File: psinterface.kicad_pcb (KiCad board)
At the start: 2 copper layers, 74.8 x 45 mm, 7 parts, among them J1 Conn_02x04_Top_Bottom, J2 Conn_01x10, J3 Conn_02x06_Top_Bottom, J4 Conn_01x05, J5 Conn_01x01, J6 Conn_01x03, SW1 SW_SPDT

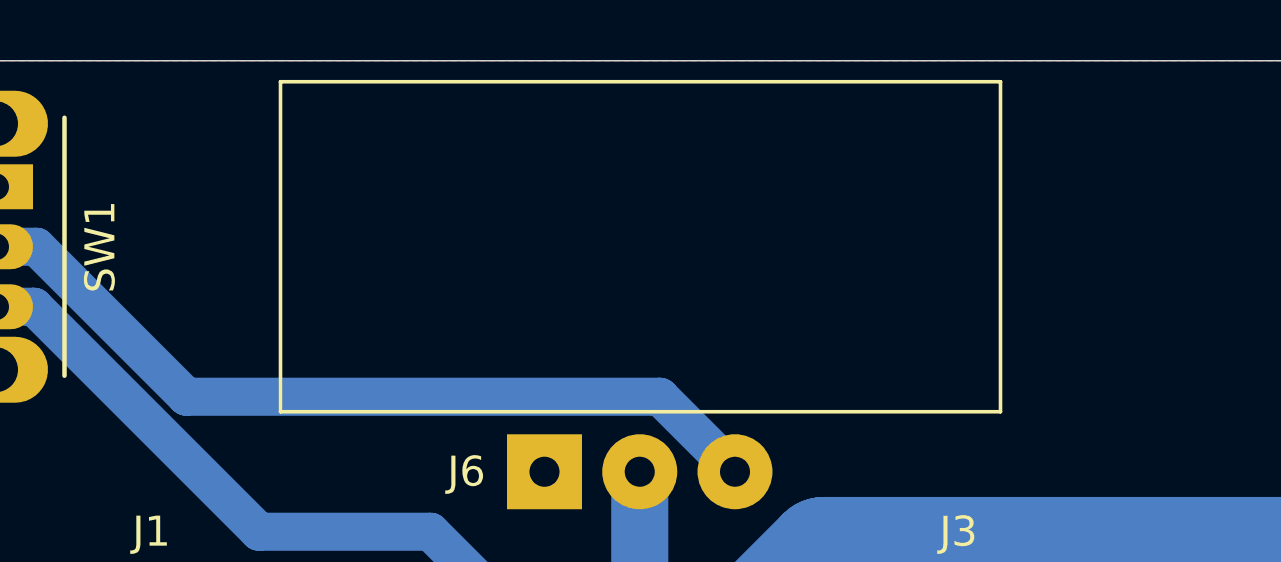
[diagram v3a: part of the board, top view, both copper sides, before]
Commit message: Mounting holes for LCD fixed
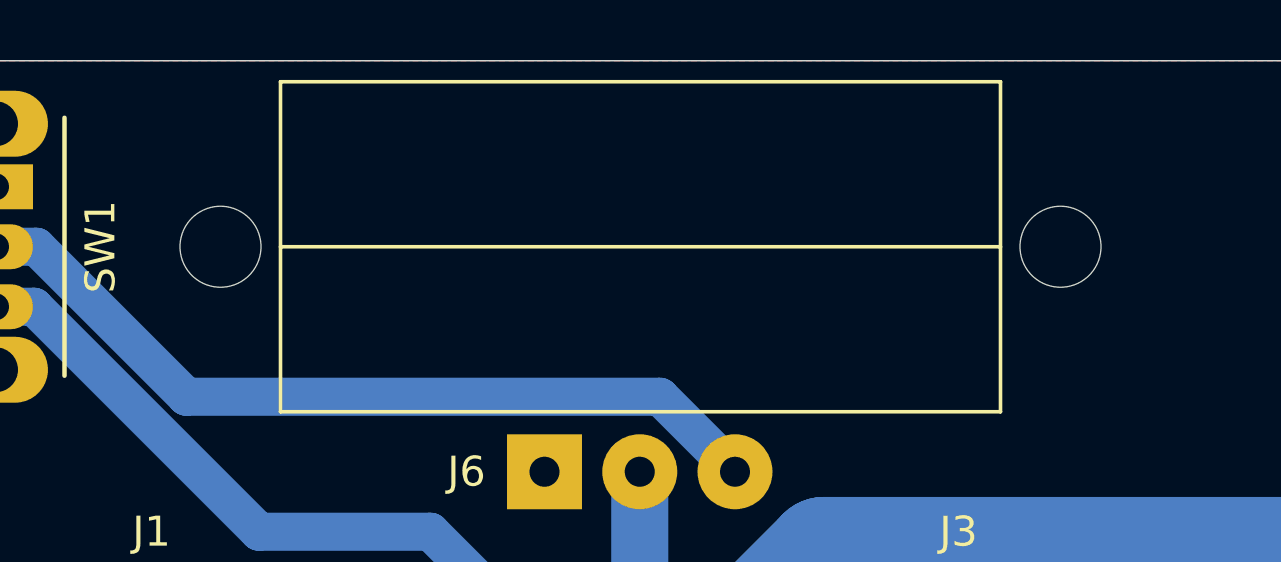
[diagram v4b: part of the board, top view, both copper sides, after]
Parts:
- added H1: MountingHole, MountingHole:MountingHole_2.7mm_M2.5, F.Cu at (115.0, 100.5)
- added H2: MountingHole, MountingHole:MountingHole_2.7mm_M2.5, F.Cu at (143.0, 100.5)
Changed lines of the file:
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@@
   (general
     (thickness 1.6)
-    (drawings 57)
+    (drawings 58)
     (tracks 74)
     (zones 0)
-    (modules 7)
+    (modules 9)
     (nets 10)
   )
@@
       (net 9 "Net-(J6-Pad3)"))
   )
+  (module MountingHole:MountingHole_2.7mm_M2.5 (layer F.Cu)
+    (at 115 100.5)
+    (descr "Mounting Hole 2.7mm, no annular, M2.5")
+    (tags "mounting hole 2.7mm no annular m2.5")
+    (attr virtual)
+    (fp_text reference H1 (at 0 -3.7) (layer F.SilkS) hide
+      (effects (font (size 1 1) (thickness 0.15)))
+    )
+    (fp_text value MountingHole (at 0 3.7) (layer F.Fab)
+      (effects (font (size 1 1) (thickness 0.15)))
+    )
+    (fp_text user %R (at 0.3 0) (layer F.Fab)
+      (effects (font (size 1 1) (thickness 0.15)))
+    )
+    (fp_circle (center 0 0) (end 2.7 0) (layer Cmts.User) (width 0.15))
+    (fp_circle (center 0 0) (end 2.95 0) (layer F.CrtYd) (width 0.05))
+    (pad 1 np_thru_hole circle (at 0 0) (size 2.7 2.7) (drill 2.7) (layers *.Cu *.Mask))
+  )
+  (module MountingHole:MountingHole_2.7mm_M2.5 (layer F.Cu)
+    (at 143 100.5)
+    (descr "Mounting Hole 2.7mm, no annular, M2.5")
+    (tags "mounting hole 2.7mm no annular m2.5")
+    (attr virtual)
+    (fp_text reference H2 (at 0 -3.7) (layer F.SilkS) hide
+      (effects (font (size 1 1) (thickness 0.15)))
+    )
+    (fp_text value MountingHole (at 0 3.7) (layer F.Fab)
+      (effects (font (size 1 1) (thickness 0.15)))
+    )
+    (fp_circle (center 0 0) (end 2.95 0) (layer F.CrtYd) (width 0.05))
+    (fp_circle (center 0 0) (end 2.7 0) (layer Cmts.User) (width 0.15))
+    (fp_text user %R (at 0.3 0) (layer F.Fab)
+      (effects (font (size 1 1) (thickness 0.15)))
+    )
+    (pad 1 np_thru_hole circle (at 0 0) (size 2.7 2.7) (drill 2.7) (layers *.Cu *.Mask))
+  )
+  (gr_line (start 141 100.5) (end 117 100.5) (layer F.SilkS) (width 0.12))
   (gr_text "Meanwell\nQP-150-3A\nAWSD Interface" (at 168 97.5) (layer F.SilkS)
     (effects (font (size 1 1) (thickness 0.15)))

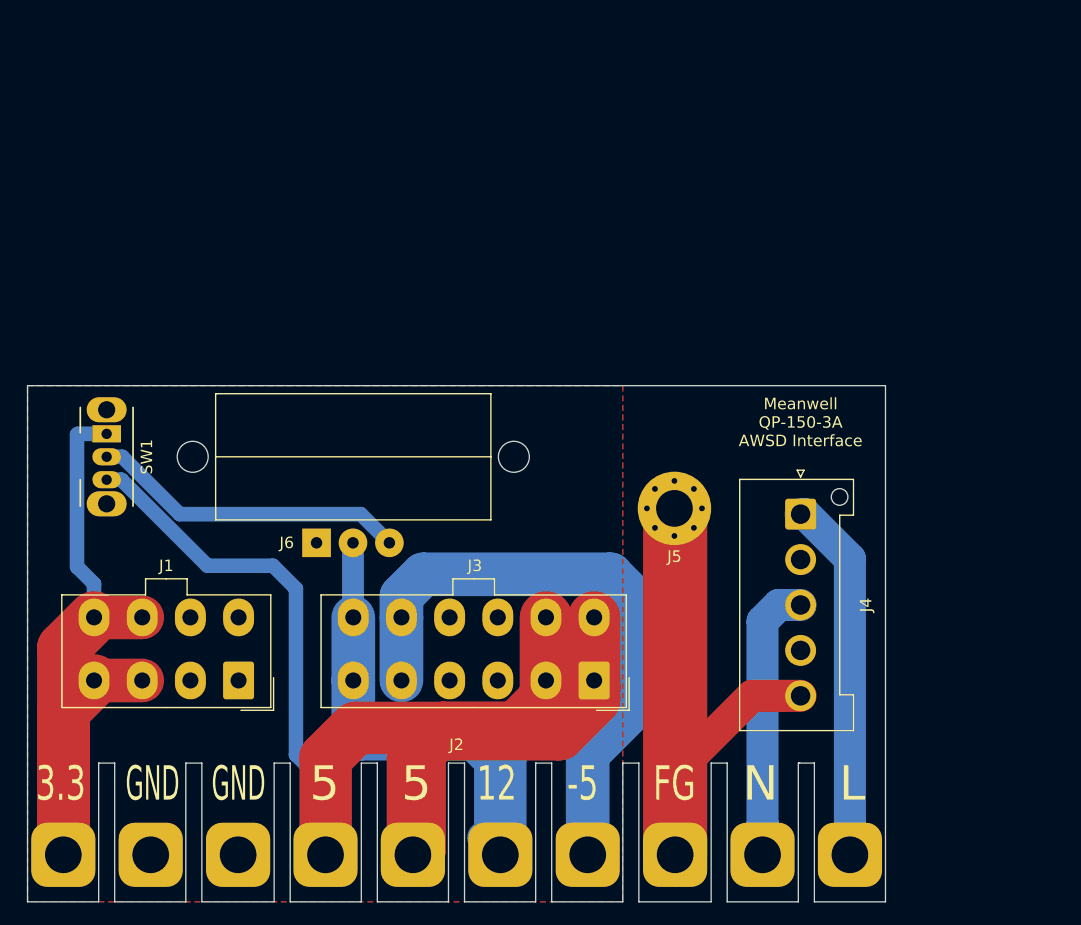
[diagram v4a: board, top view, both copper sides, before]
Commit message: Rounded flanges, fixed wiring
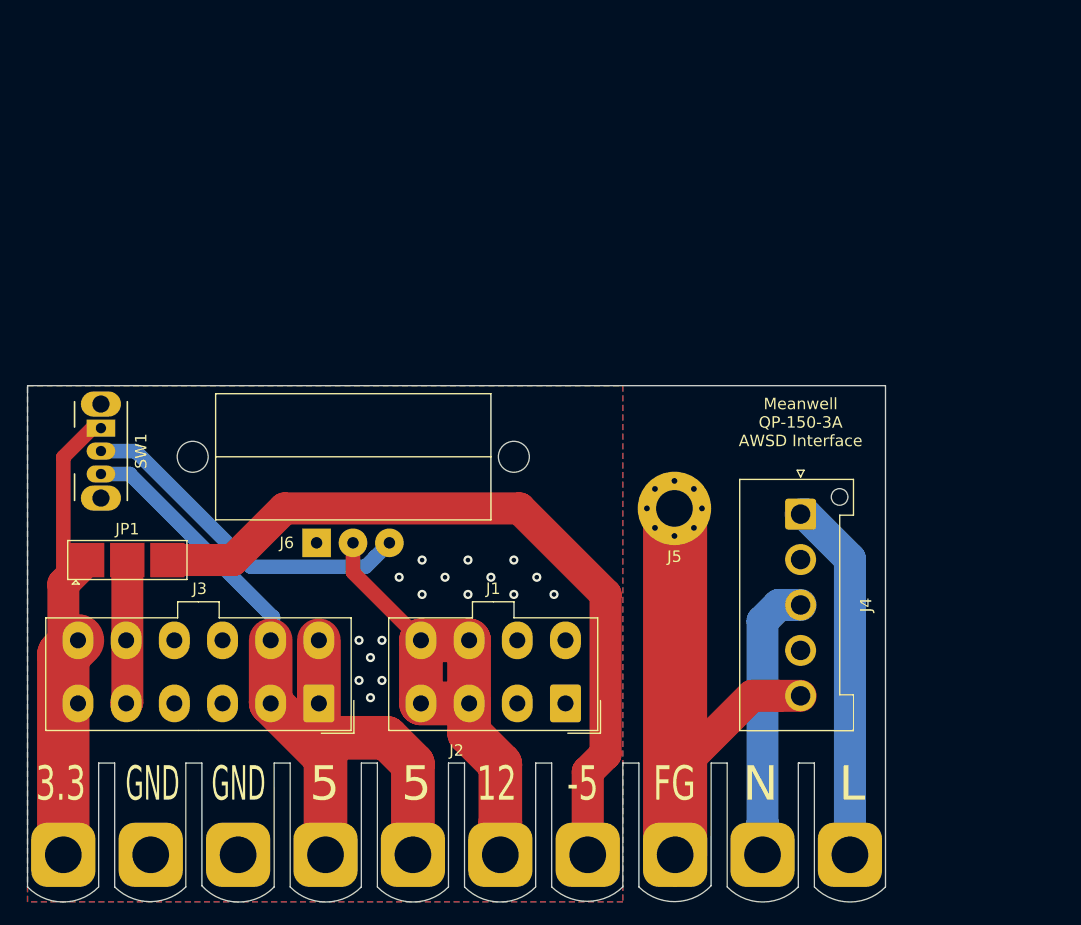
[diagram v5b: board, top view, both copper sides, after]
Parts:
- added JP1: SolderJumper_3_Open, Andrew-Custom:SolderJumper-3_P3.5mm_Open_Pad3.0x3.0mm, F.Cu at (109.3, 109.5)
- moved J1 28.6 mm to (147.5, 122.0)
- moved J3 24.1 mm to (126.0, 122.0)
- moved SW1 0.71 mm to (107.0, 98.0)
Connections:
- net Net-(J1-Pad1) renamed /GND
- net Net-(J2-Pad10) renamed /AC-L
- net Net-(J2-Pad4) renamed /5.25V
- net Net-(J2-Pad8) renamed /AC-FG
- net Net-(J2-Pad9) renamed /AC-N
- J1 pad 3: Net-(J1-Pad3) -> /12V
- J1 pad 4: Net-(J1-Pad3) -> /12V
- J1 pad 7: Net-(J1-Pad3) -> /12V
- J1 pad 8: Net-(J1-Pad3) -> /12V
- J2 pad 1: Net-(J1-Pad3) -> /3.3V
- J2 pad 6: Net-(J2-Pad6) -> /12V
- J2 pad 7: Net-(J2-Pad7) -> /-5V
- J3 pad 11: Net-(J2-Pad7) -> Net-(J3-Pad11)
- J3 pad 12: Net-(J2-Pad6) -> /3.3V
- J3 pad 5: Net-(J2-Pad7) -> Net-(J3-Pad11)
- J3 pad 6: Net-(J2-Pad6) -> /3.3V
- J6 pad 2: Net-(J2-Pad6) -> /12V
- SW1 pad 1: Net-(J1-Pad3) -> /3.3V
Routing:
- net /3.3V: track 0.00 -> 84.8 mm
- net /5.25V: track 142.6 -> 68.2 mm
- net /-5V: track 0.00 -> 66.5 mm
- net Net-(J1-Pad3): track 65.7 -> 0.00 mm
- net Net-(J2-Pad7): track 53.3 -> 0.00 mm
- net /12V: track 0.00 -> 44.7 mm
- net Net-(J2-Pad6): track 40.6 -> 0.00 mm
- net Net-(J3-Pad11): track 0.00 -> 12.5 mm
- net Net-(J6-Pad3): track 27.8 -> 30.2 mm
- net /GND: vias 0 -> 17
- added copper zone on B.Cu, net /GND
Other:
- outline, holes or cut-outs redrawn

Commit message: Better use of bottom copper
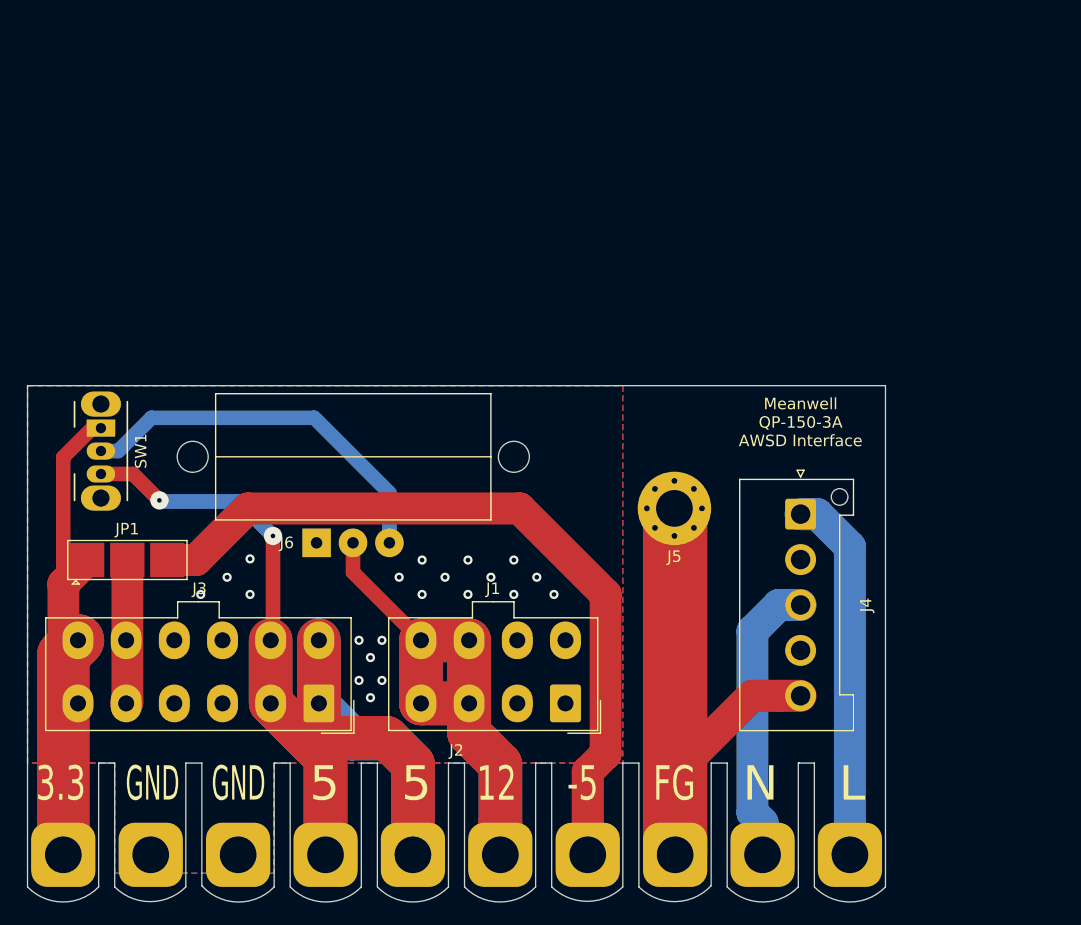
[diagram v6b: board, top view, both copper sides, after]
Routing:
- net /5.25V: track 68.2 -> 117.3 mm, vias 0 -> 2
- net /12V: track 44.7 -> 78.4 mm
- net /AC-FG: track 51.1 -> 81.3 mm
- net /3.3V: track 84.8 -> 104.0 mm
- net Net-(J6-Pad3): track 30.2 -> 33.4 mm
- net /AC-N: track 24.3 -> 25.0 mm
- net /AC-L: track 31.7 -> 32.3 mm
- net /GND: vias 17 -> 21

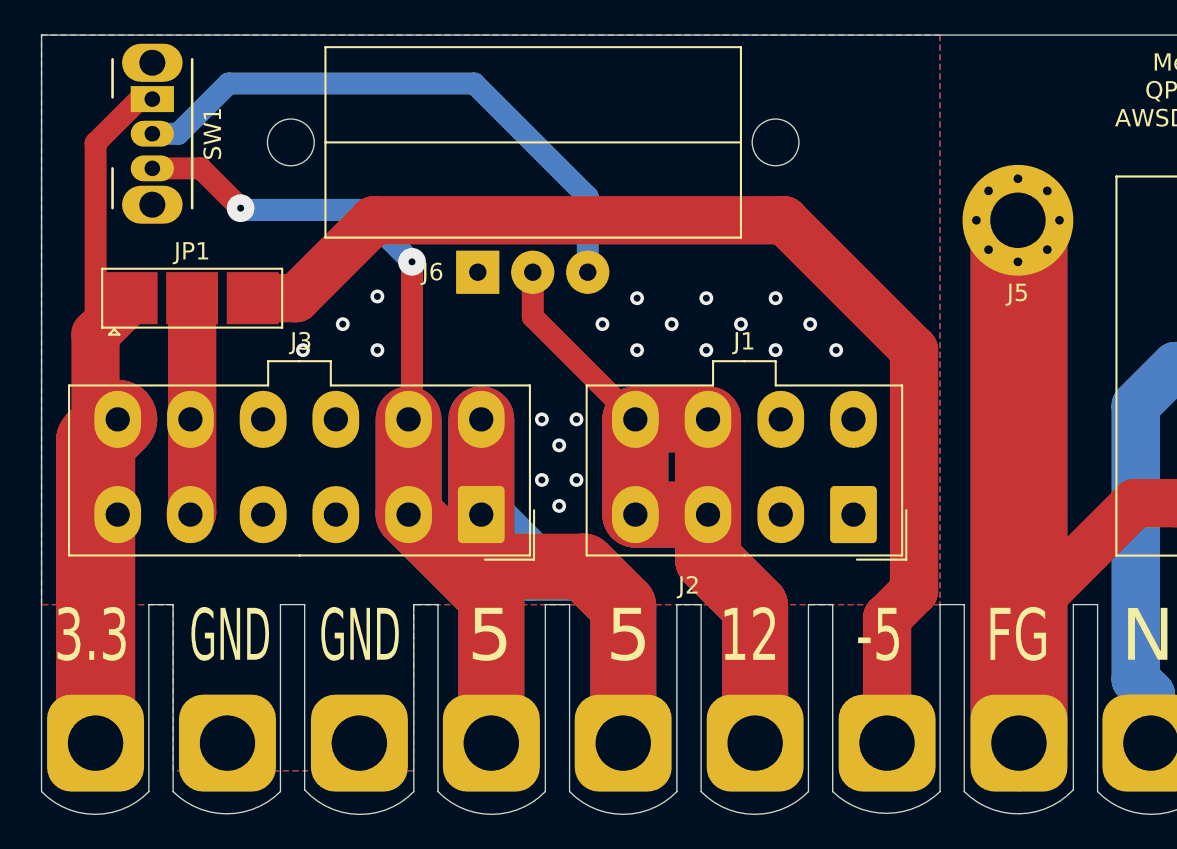
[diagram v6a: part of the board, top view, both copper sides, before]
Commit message: J6 now 4MM, JP2/3 added to allow diff polarity LCD
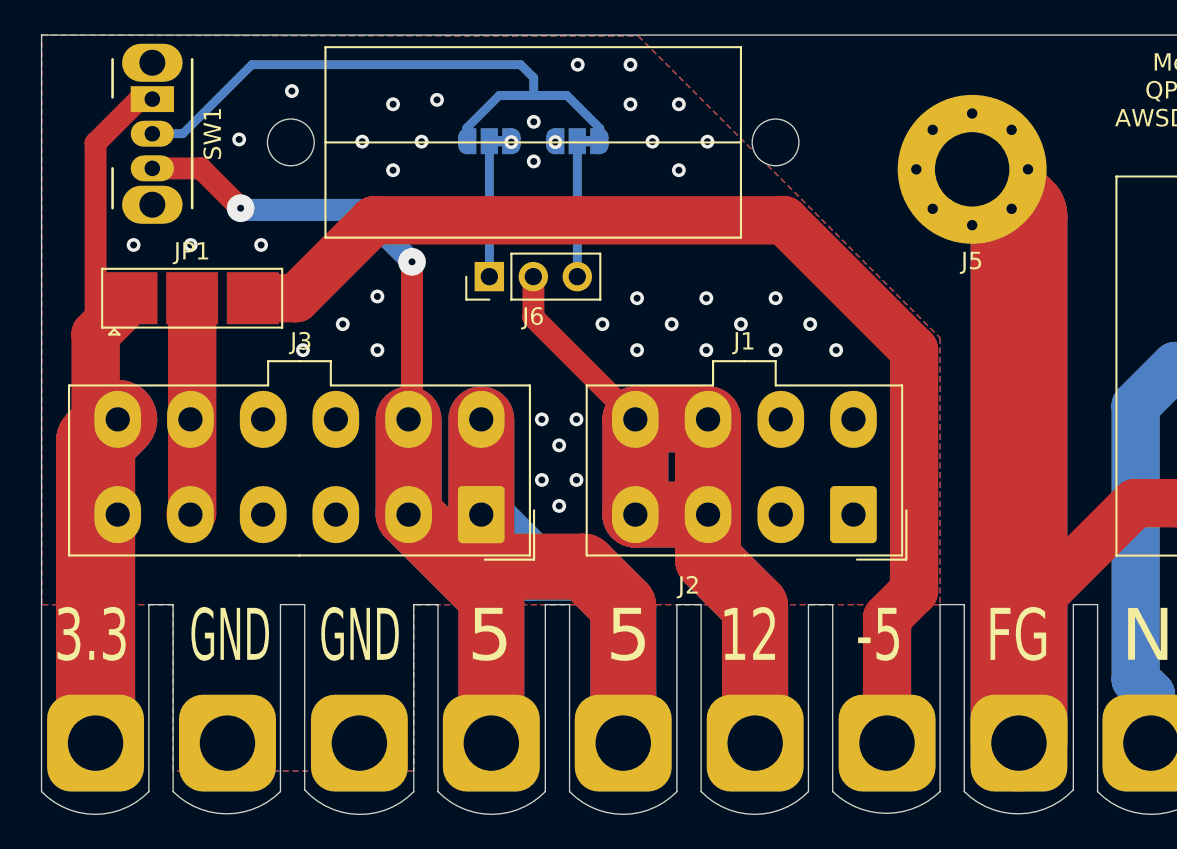
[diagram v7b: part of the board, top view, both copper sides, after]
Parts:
- added JP2: JP, Jumper:SolderJumper-3_P1.3mm_Bridged12_RoundedPad1.0x1.5mm, B.Cu at (126.5, 100.4)
- added JP3: JP, Jumper:SolderJumper-3_P1.3mm_Bridged12_RoundedPad1.0x1.5mm, B.Cu at (131.5, 100.4)
- J5: footprint MountingHole:MountingHole_3.2mm_M3_Pad_Via -> MountingHole:MountingHole_4.3mm_M4_Pad_Via
- J6: footprint Connector_Wire:SolderWirePad_1x03_P3.175mm_Drill1mm -> Connector_PinHeader_2.54mm:PinHeader_1x03_P2.54mm_Vertical
- moved J5 3.96 mm to (154.4, 102.1)
- moved J6 0.71 mm to (126.5, 108.3), turned to 90 degrees
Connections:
- J6 pad 1: /GND -> Net-(J6-Pad1)
- SW1 pad 2: Net-(J6-Pad3) -> Net-(JP2-Pad3)
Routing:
- net Net-(JP2-Pad3): track 0.00 -> 35.8 mm
- net Net-(J6-Pad3): track 33.4 -> 7.82 mm
- net /AC-FG: track 81.3 -> 89.4 mm
- net Net-(J6-Pad1): track 0.00 -> 7.82 mm
- net /GND: vias 21 -> 42
